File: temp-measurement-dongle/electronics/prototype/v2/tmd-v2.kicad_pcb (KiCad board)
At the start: 2 copper layers, 75 x 101 mm, 90 parts, among them J1 USB2UART, J2 1.47 IPS LCD, J3 ConnBattery, J4 RTD_PT100, J5 lcd jumper, J6 lcd jumper, J7 lcd jumper, Q1 SS8050, Q2 SS8050, Q3 SS8050, Q5 SS8050, SW1 RST, SW2 IN1, SW3 Boot, SW4 IN2, SW5 IN4, SW6 IN4, SW7 IN5, SW8 IN6, U1 CH340C, U2 ESP32-S3-WROOM-1, U3 TPS63001_SEPIC_3V3, U4 MAX31865xTP, U5 BQ24075RGT_DPPM, U7 BQ27421YZFR-G1A

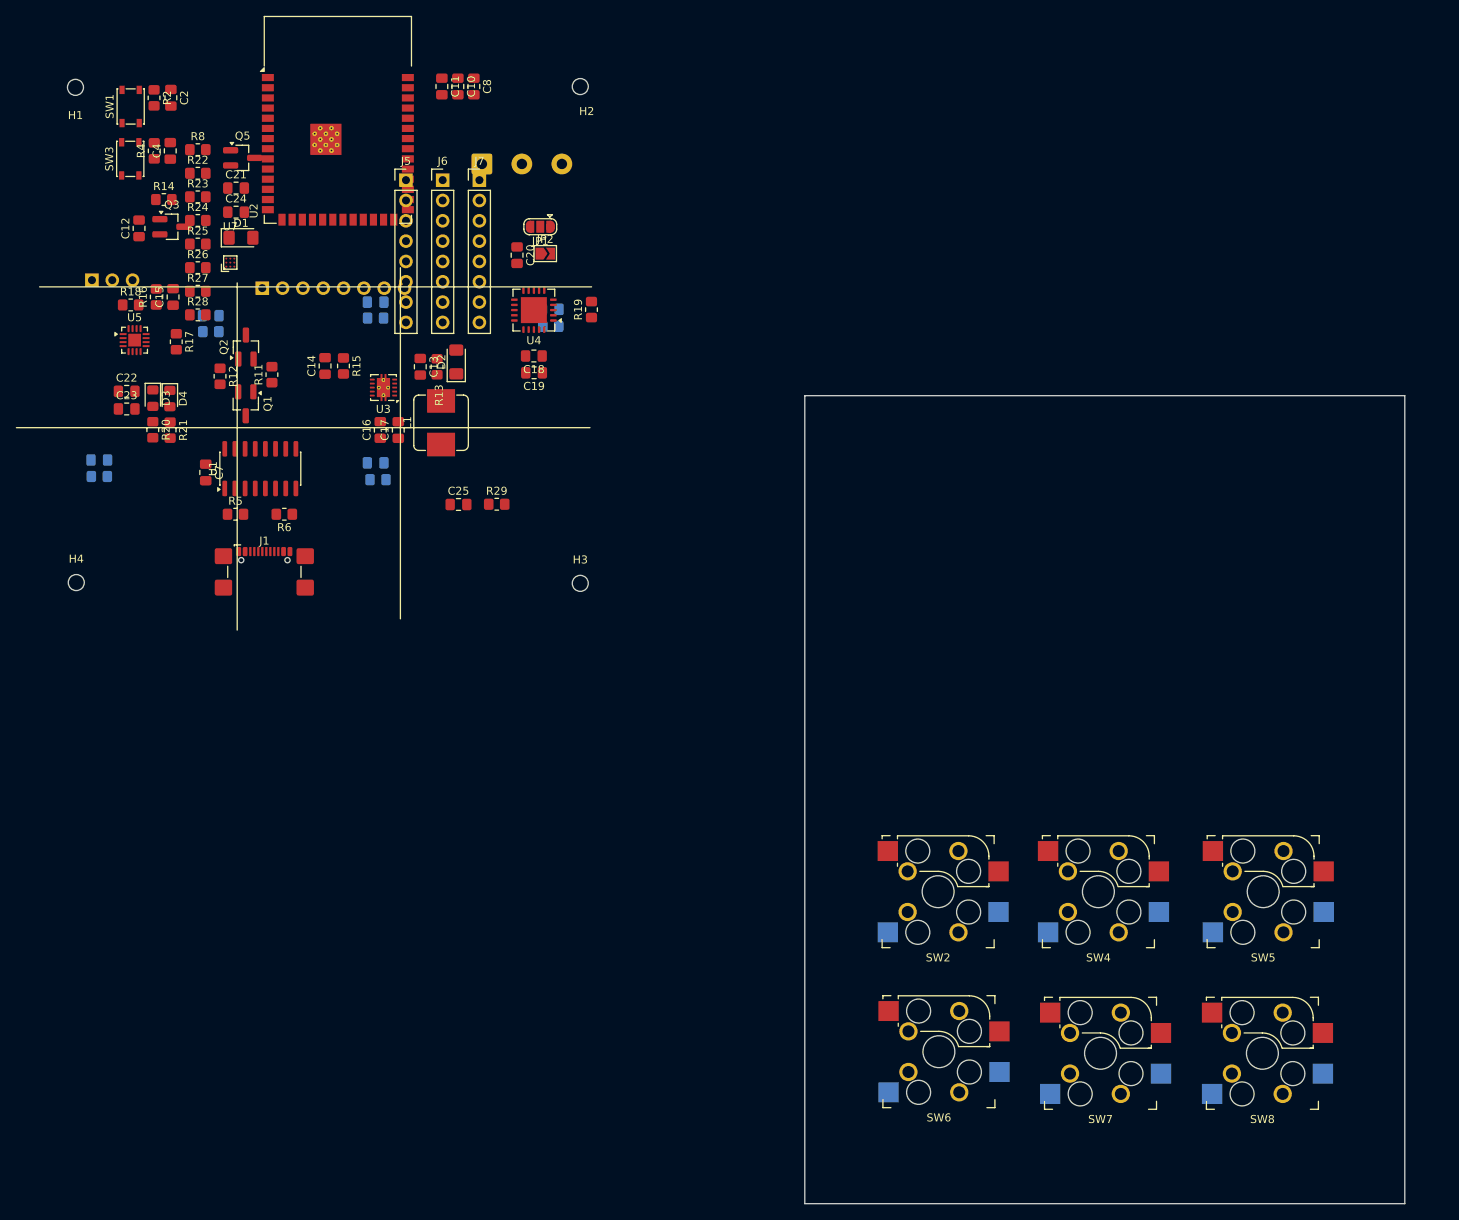
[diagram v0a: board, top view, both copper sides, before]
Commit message: use pcb shape from solidwork
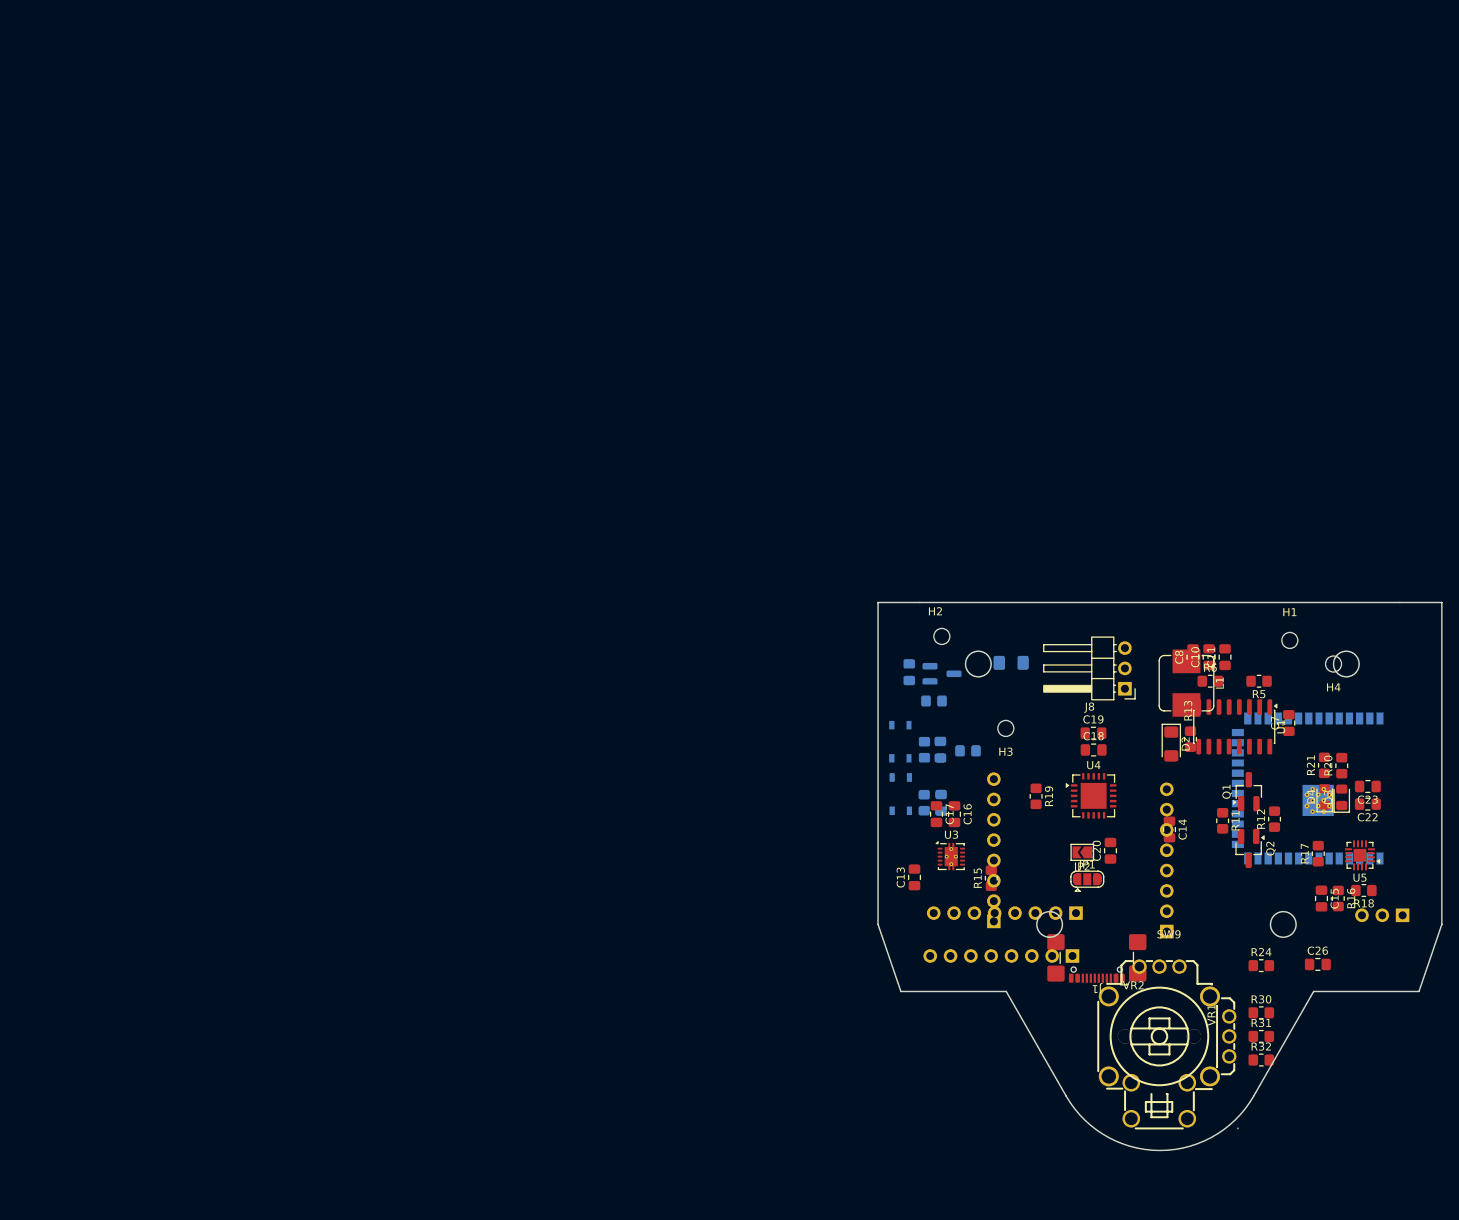
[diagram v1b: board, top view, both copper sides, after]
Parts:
- removed C1, C24, C25, C3, C5, C6, C9: 100nF, Capacitor_SMD:C_0805_2012Metric_Pad1.18x1.45mm_HandSolder
- removed C21: 0.47uF, Capacitor_SMD:C_0805_2012Metric_Pad1.18x1.45mm_HandSolder
- removed J4: RTD_PT100, TerminalBlock_Phoenix:TerminalBlock_Phoenix_PT-1,5-3-5.0-H_1x03_P5.00mm_Horizontal
- removed Q5: SS8050, Package_TO_SOT_SMD:SOT-23_Handsoldering
- removed R1, R10, R27, R29, R3, R7, R9: 1k, Resistor_SMD:R_0805_2012Metric_Pad1.20x1.40mm_HandSolder
- removed R22, R23: 4K7, Resistor_SMD:R_0805_2012Metric_Pad1.20x1.40mm_HandSolder
- removed R25, R26: 10K, Resistor_SMD:R_0805_2012Metric_Pad1.20x1.40mm_HandSolder
- removed R28: 10k, Resistor_SMD:R_0805_2012Metric_Pad1.20x1.40mm_HandSolder
- removed SW2: IN1, keyswitches.pretty-master:Kailh_socket_MX_optional_reversible_platemount
- removed SW4: IN2, keyswitches.pretty-master:Kailh_socket_MX_optional_reversible_platemount
- removed SW5, SW6: IN4, keyswitches.pretty-master:Kailh_socket_MX_optional_reversible_platemount
- removed SW7: IN5, keyswitches.pretty-master:Kailh_socket_MX_optional_reversible_platemount
- removed SW8: IN6, keyswitches.pretty-master:Kailh_socket_MX_optional_reversible_platemount
- removed U7: BQ27421YZFR-G1A, easyeda2kicad:DSBGA-9_L1.5-W1.5-R3-C3-P0.50-BL
- added C26: 100nF, Capacitor_SMD:C_0805_2012Metric_Pad1.18x1.45mm_HandSolder, F.Cu at (164.1, 112.1)
- added J8: RTD_PT100, Connector_PinHeader_2.54mm:PinHeader_1x03_P2.54mm_Horizontal, F.Cu at (140.0, 77.6)
- added R30: 1k, Resistor_SMD:R_0805_2012Metric_Pad1.20x1.40mm_HandSolder, F.Cu at (157.1, 118.1)
- added R31: 1k, Resistor_SMD:R_0805_2012Metric_Pad1.20x1.40mm_HandSolder, F.Cu at (157.1, 121.1)
- added R32: 1k, Resistor_SMD:R_0805_2012Metric_Pad1.20x1.40mm_HandSolder, F.Cu at (157.1, 124.0)
- added SW9: PS Joystick, easyeda2kicad:SW-TH_RKJXV1224005, F.Cu at (145.5, 121.9)
- C12, C2, C4, D1, J5, Q3, R14, R2, R4, R8, SW1, SW3, U2: moved to B.Cu
- J6, J7: footprint Connector_PinHeader_2.54mm:PinHeader_1x08_P2.54mm_Vertical -> Connector_PinHeader_2.54mm:PinHeader_1x08_P2.54mm_Horizontal; moved to B.Cu
- R24: value 10k -> 200
- moved J3 182.1 mm to (174.7, 106.0), turned to 90 degrees
- moved R18 170.6 mm to (169.9, 102.9), turned to 180 degrees
- moved H1 166.8 mm to (160.6, 71.6), turned to 180 degrees
- moved U5 166.2 mm to (169.4, 98.5), turned to 180 degrees
- moved R16 165.8 mm to (166.7, 103.9), turned to -90 degrees
- moved C22 163.5 mm to (170.4, 92.1), turned to 180 degrees
- moved R24 162.3 mm to (157.1, 112.2)
- moved C23 162.2 mm to (170.4, 89.9), turned to 180 degrees
- moved C15 162.1 mm to (164.6, 103.9), turned to -90 degrees
- moved H4 157.5 mm to (166.1, 74.5), turned to 180 degrees
- moved D3 156.8 mm to (167.1, 91.2), turned to 90 degrees
- moved R17 156.4 mm to (164.2, 98.3), turned to 90 degrees
- moved R20 154.4 mm to (167.1, 87.3), turned to 90 degrees
- moved D4 152.7 mm to (165.0, 91.2), turned to 90 degrees
- moved U2 150.4 mm to (166.6, 90.1), turned to 90 degrees
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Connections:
- Q3 pad 1: /~{CHG} -> Net-(Q3-B)
- R24 pad 1: +3.3V -> Net-(Q3-B)
- U2 pad 10: /IN1 -> /AN2
- U2 pad 11: /IN2 -> /AN1
- U2 pad 13: /IN3 -> /ANSW
- U2 pad 14: /IN4 -> unconnected-(U2-IO20-Pad14)
- U2 pad 23: /IN5 -> unconnected-(U2-IO21-Pad23)
- U2 pad 33: /IN6 -> unconnected-(U2-IO40-Pad33)
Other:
- board size 75 x 101 mm -> 70.5 x 68.5 mm

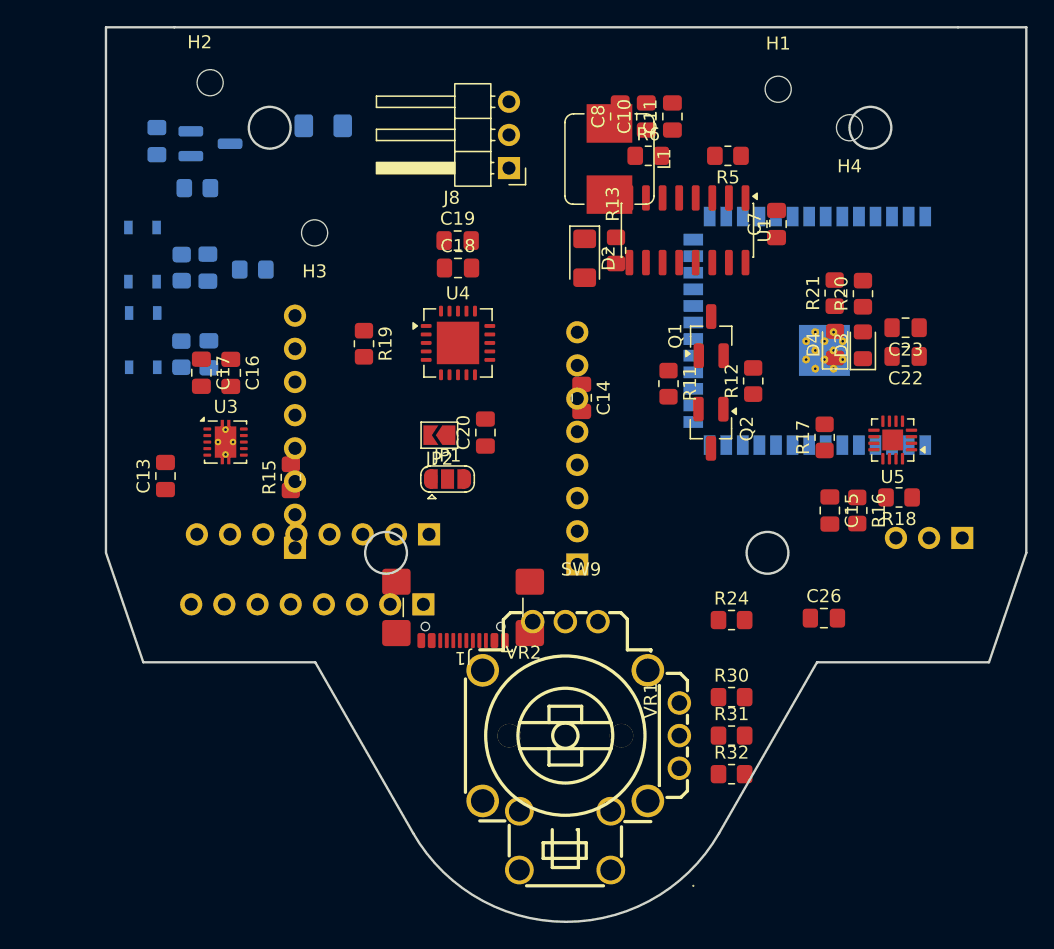
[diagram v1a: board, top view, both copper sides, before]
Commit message: re-positioning component
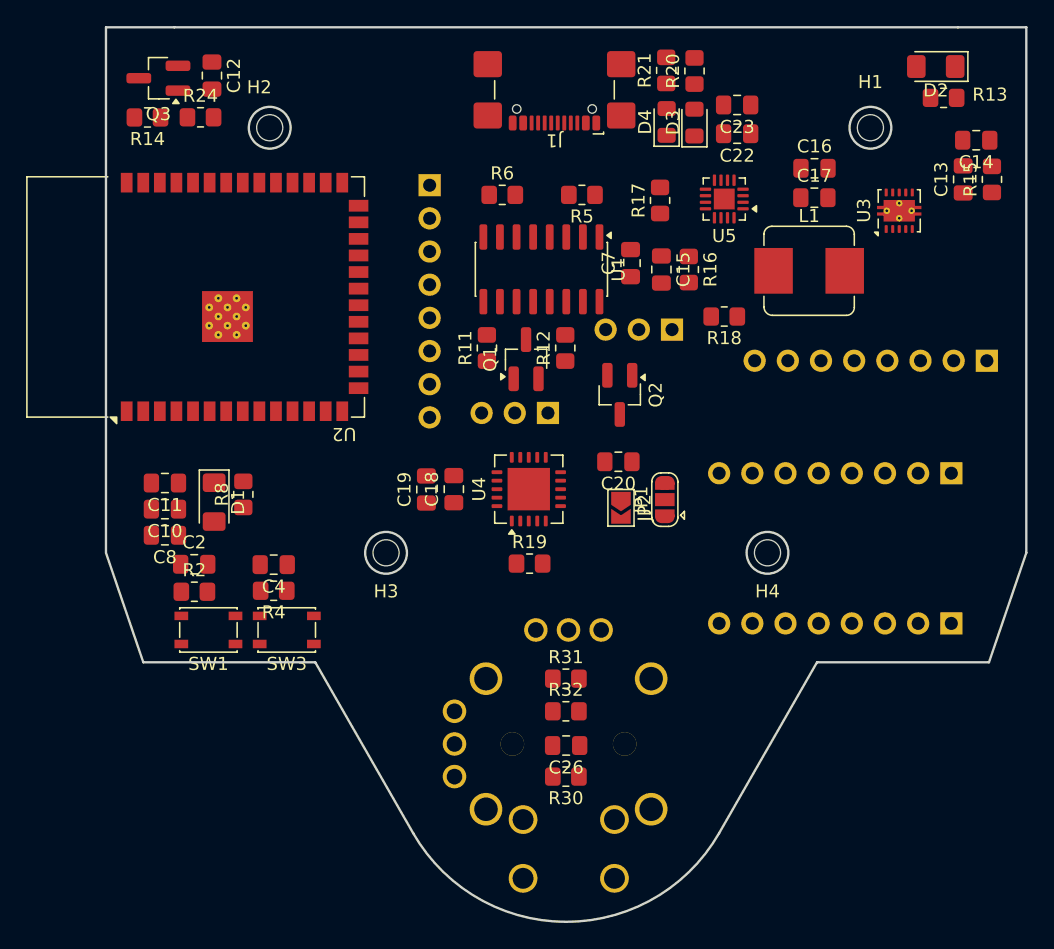
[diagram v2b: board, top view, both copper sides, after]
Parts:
- C12, C2, C4, D1, Q3, R14, R2, R4, R8, SW1, SW3, U2: moved to F.Cu
- J3: footprint Connector_PinHeader_2.54mm:PinHeader_1x03_P2.54mm_Vertical -> Connector_PinHeader_2.54mm:PinHeader_1x03_P2.54mm_Horizontal
- J6: footprint Connector_PinHeader_2.54mm:PinHeader_1x08_P2.54mm_Horizontal -> Connector_PinHeader_2.54mm:PinHeader_1x08_P2.54mm_Vertical
- J8, SW9: moved to B.Cu
- moved C13 65.2 mm to (174.8, 78.5)
- moved R15 58.3 mm to (177.0, 78.5)
- moved R24 56.0 mm to (116.4, 73.7)
- moved U3 54.5 mm to (169.9, 80.9), turned to 90 degrees
- moved U2 50.7 mm to (116.0, 87.5)
- moved J6 50.6 mm to (173.9, 101.0), turned to 90 degrees
- moved C17 48.8 mm to (163.4, 79.9), turned to 0 degrees
- moved C11 47.9 mm to (113.7, 101.8), turned to 180 degrees
- moved C10 47.6 mm to (113.7, 103.8), turned to 180 degrees
- moved C8 47.4 mm to (113.7, 105.8), turned to 180 degrees
- moved C16 47.4 mm to (163.4, 77.7), turned to 0 degrees
- moved J2 40.5 mm to (173.9, 112.5)
- moved J1 40.2 mm to (143.5, 70.5)
- moved C14 36.1 mm to (175.8, 75.5), turned to 180 degrees
- moved J7 35.0 mm to (176.6, 92.4), turned to 90 degrees
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
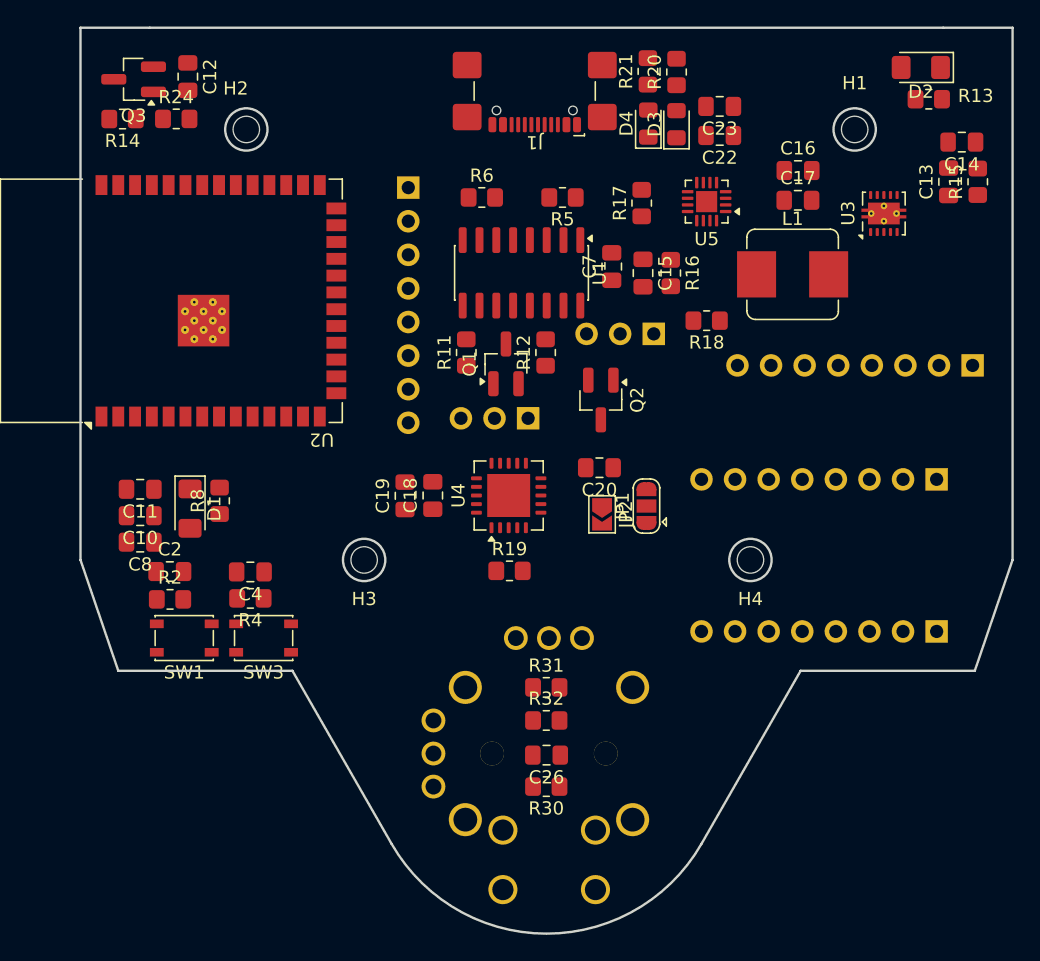
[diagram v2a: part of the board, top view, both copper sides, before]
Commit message: complete tmd v2 routing
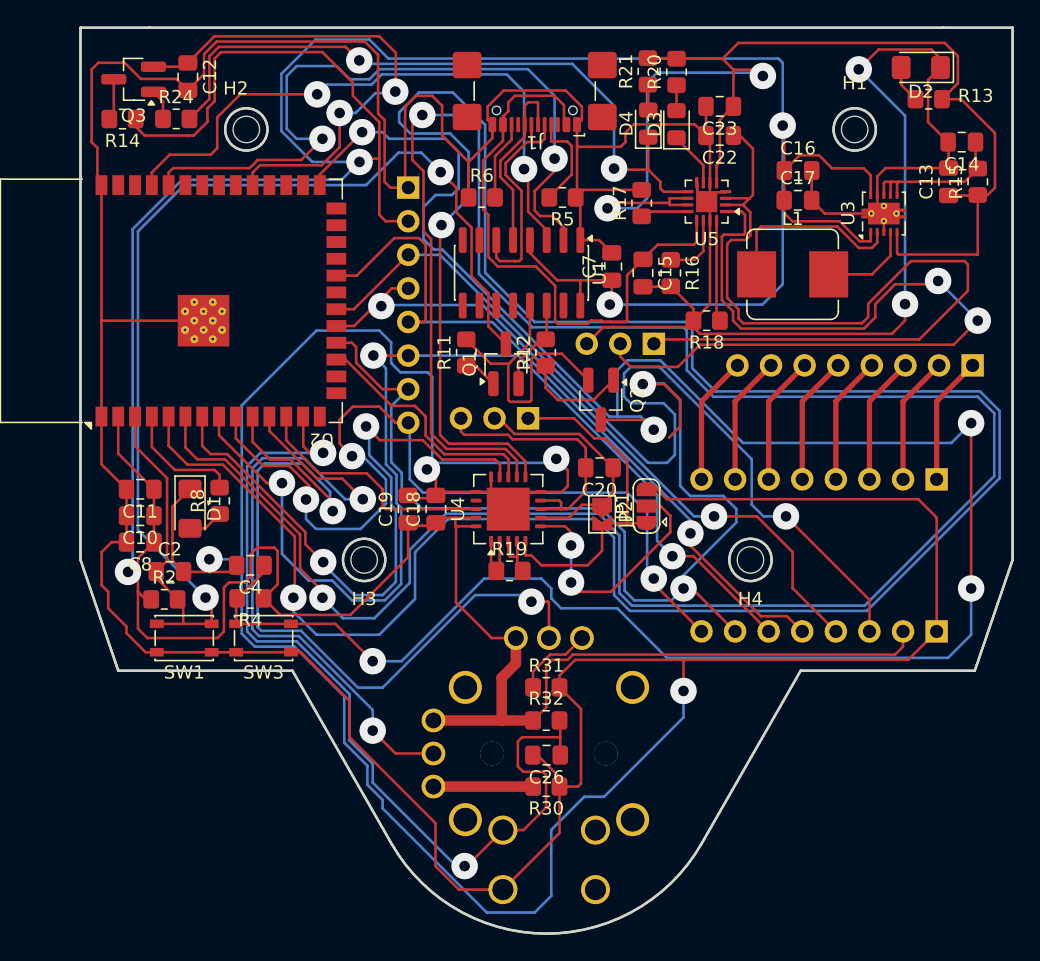
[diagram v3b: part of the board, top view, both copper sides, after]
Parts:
- moved C18 1.06 mm to (136.0, 103.2)
- moved C19 1.03 mm to (133.9, 103.2)
- moved U4 1.03 mm to (141.5, 103.2)
- moved J3 0.74 mm to (152.5, 90.7)
- moved C4 0.50 mm to (122.0, 107.5)
- moved R2 0.42 mm to (115.5, 110.1)
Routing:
- net GND: track 0.00 -> 530.4 mm, vias 0 -> 6
- net +3.3V: track 0.00 -> 323.5 mm, vias 0 -> 4
- net /MOSI2: track 0.00 -> 196.8 mm, vias 0 -> 2
- net /SCK2: track 0.00 -> 184.5 mm, vias 0 -> 2
- net /IO0: track 0.00 -> 167.7 mm, vias 0 -> 5
- net VDD: track 0.00 -> 95.3 mm, vias 0 -> 2
- net /EN: track 0.00 -> 95.0 mm, vias 0 -> 2
- net /DC: track 0.00 -> 82.7 mm, vias 0 -> 3
- net /CS: track 0.00 -> 78.0 mm, vias 0 -> 2
- net /SCK: track 0.00 -> 73.7 mm, vias 0 -> 1
- net /ANSW: track 0.00 -> 70.0 mm, vias 0 -> 2
- net +BATT: track 0.00 -> 68.4 mm
- net /BLK: track 0.00 -> 66.9 mm, vias 0 -> 3
- net /TS: track 0.00 -> 63.9 mm, vias 0 -> 2
- net /AN2: track 0.00 -> 60.3 mm, vias 0 -> 2
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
